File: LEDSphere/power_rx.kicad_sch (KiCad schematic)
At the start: 54 parts, among them U114 DRV5033FAQDBZR, U3 TPS54202HDDCR, U4 TPS54202HDDCR

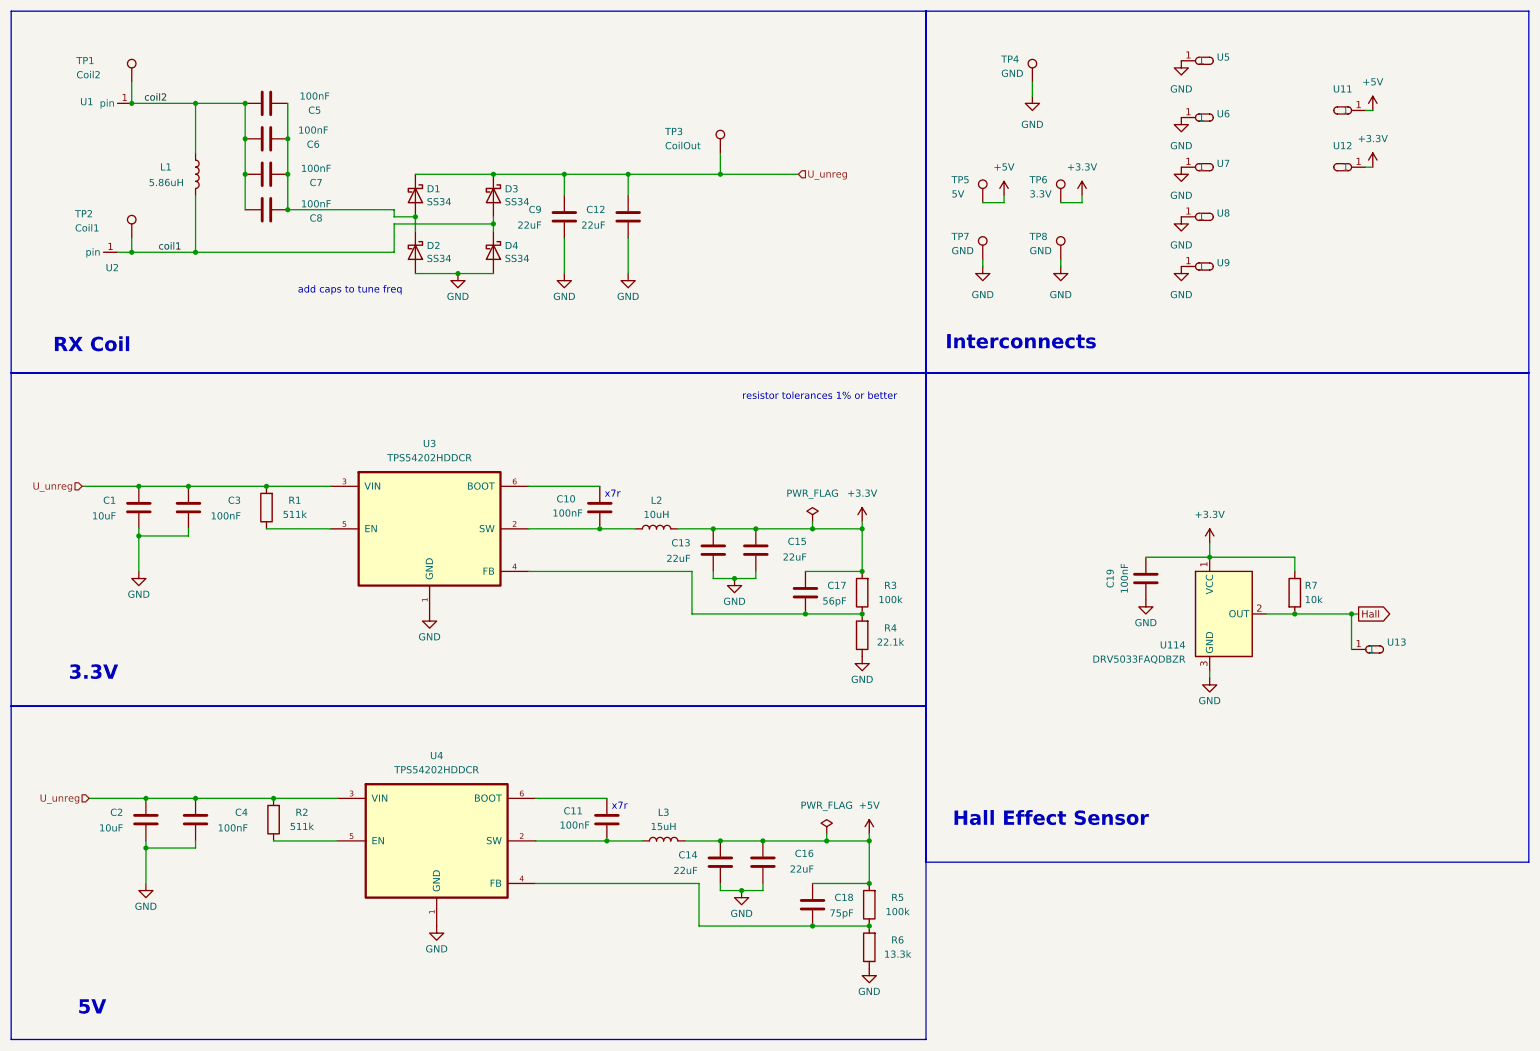
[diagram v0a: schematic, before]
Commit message: add leds
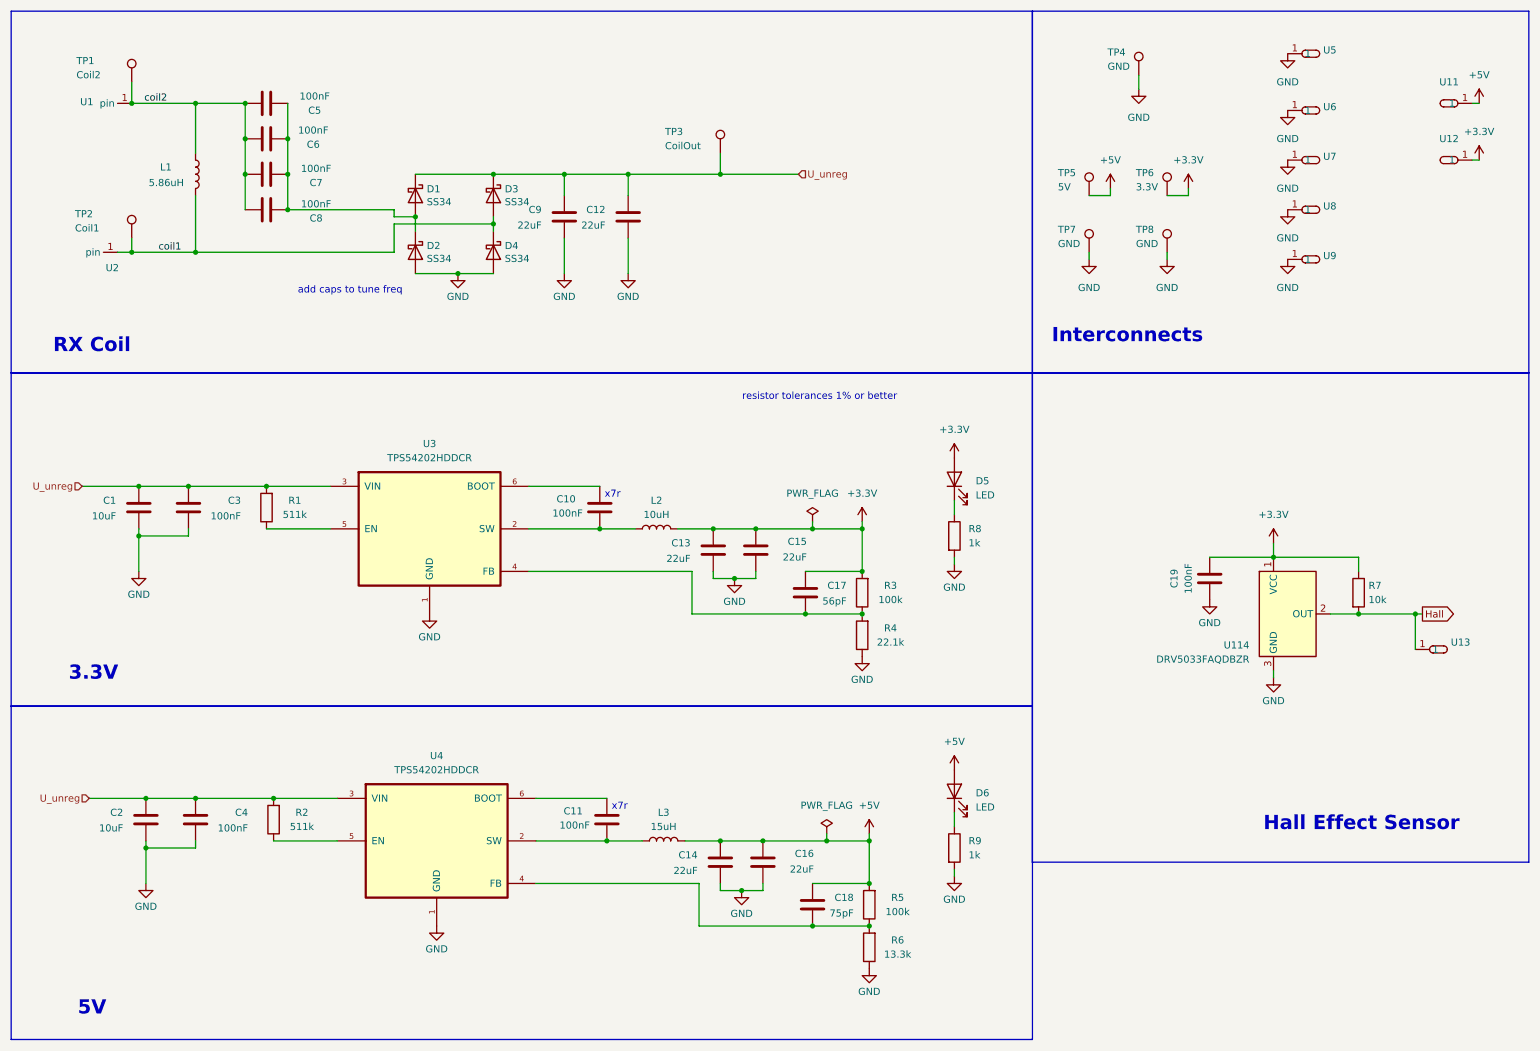
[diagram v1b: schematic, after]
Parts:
- added D5, D6: LED, LED_SMD:LED_0805_2012Metric, symbol Device:LED
- added R8, R9: 1k, Resistor_SMD:R_0603_1608Metric, symbol Device:R
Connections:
- net +3.3V: now also D5.2 (A)
- net +5V: now also D6.2 (A)
- net GND: now also R8.2, R9.2
- new net: D5.1 (K), R8.1
- new net: D6.1 (K), R9.1
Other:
- moved on the sheet: C19, R7, TP4, TP5, TP6, TP7, TP8, U11, U114, U12, U13, U5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
